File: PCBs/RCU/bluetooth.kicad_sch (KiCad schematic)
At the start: 14 parts

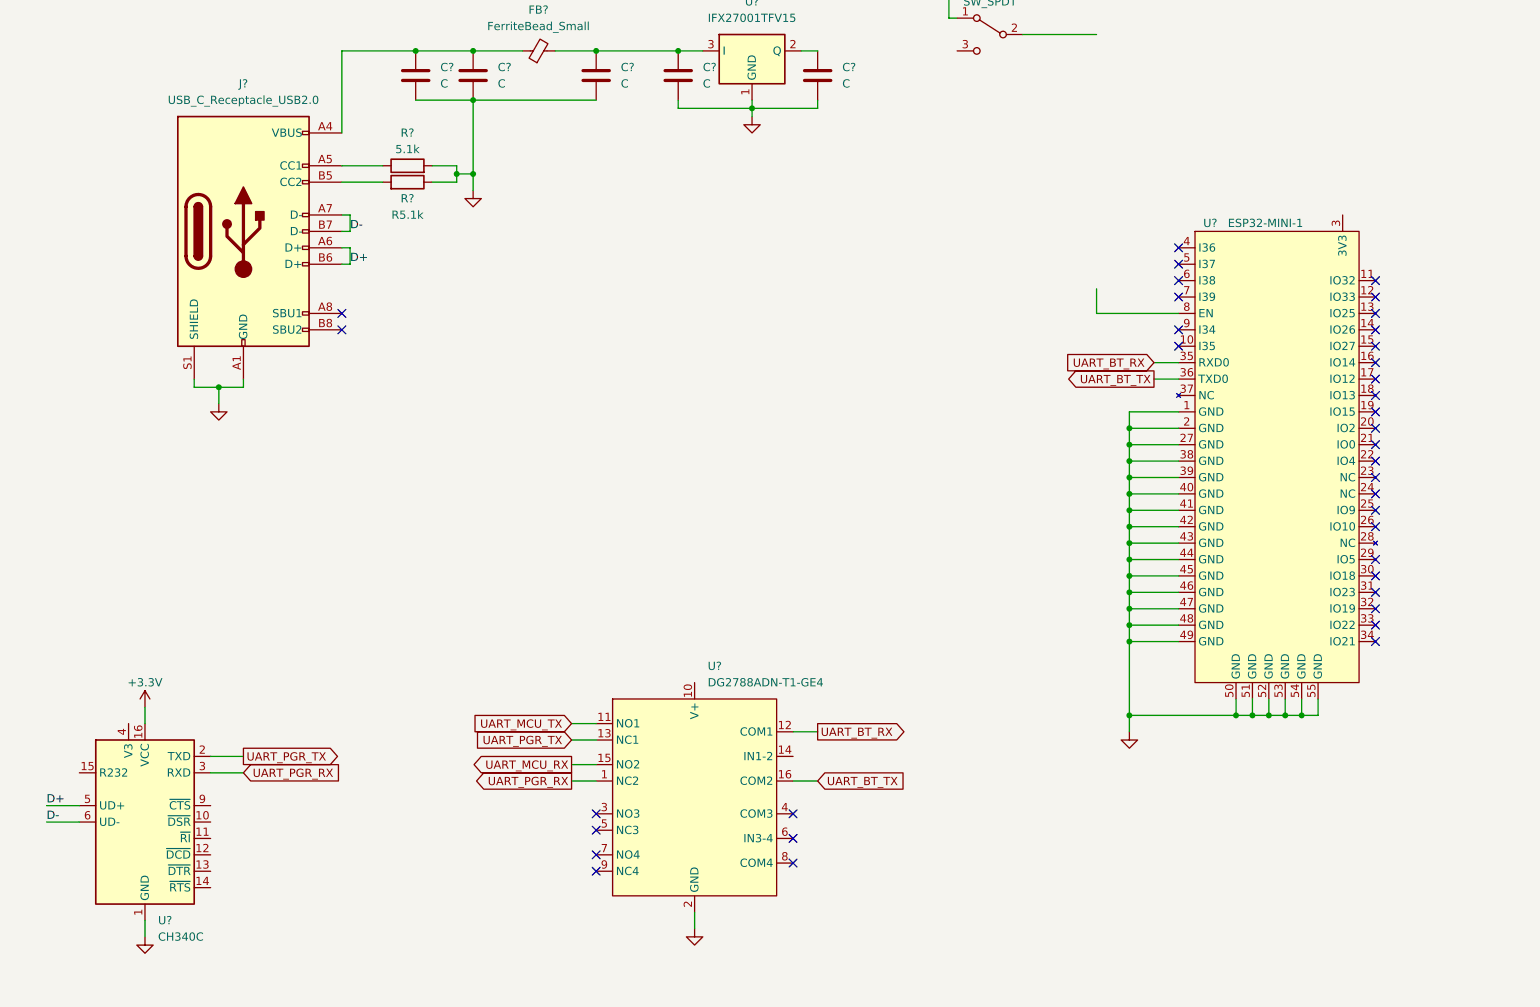
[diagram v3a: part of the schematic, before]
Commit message: Completed UART multiplexer circuit
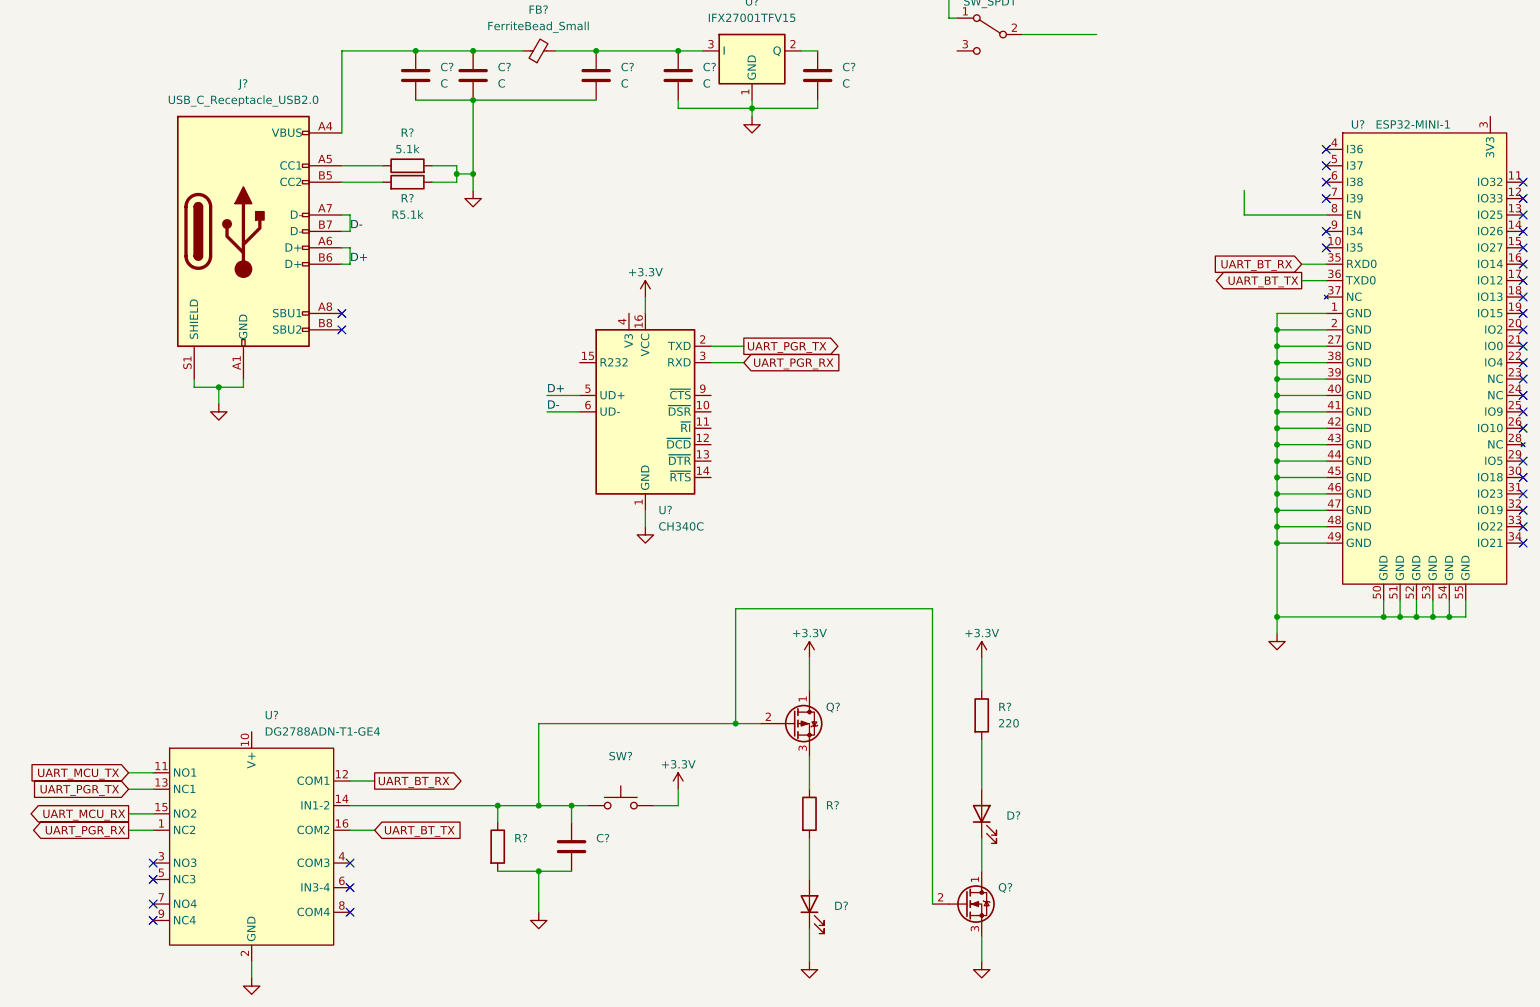
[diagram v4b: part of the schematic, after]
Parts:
- added C?: (no value), symbol Device:C
- added D? (x2): (no value), symbol Device:LED
- added Q?: (no value), symbol Device:Q_PMOS_DGS
- added Q?: (no value), symbol Device:Q_NMOS_DGS
- added R? (x2): (no value), symbol Device:R
- added R?: 220, symbol Device:R
- added SW?: (no value), symbol Switch:SW_Push
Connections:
- net +3V3: now also Q?.1 (D), R?.1, SW?.2
- net GND: now also C?.2, D?.1 (K), Q?.3 (S), R?.2
- net at U?.14 (IN1-2): now also C?.1, Q?.2 (G), Q?.2 (G), R?.1, SW?.1
- new net: Q?.3 (S), R?.1
- new net: D?.2 (A), R?.2 (x2)
- new net: D?.1 (K), Q?.1 (D)
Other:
- moved on the sheet: U?

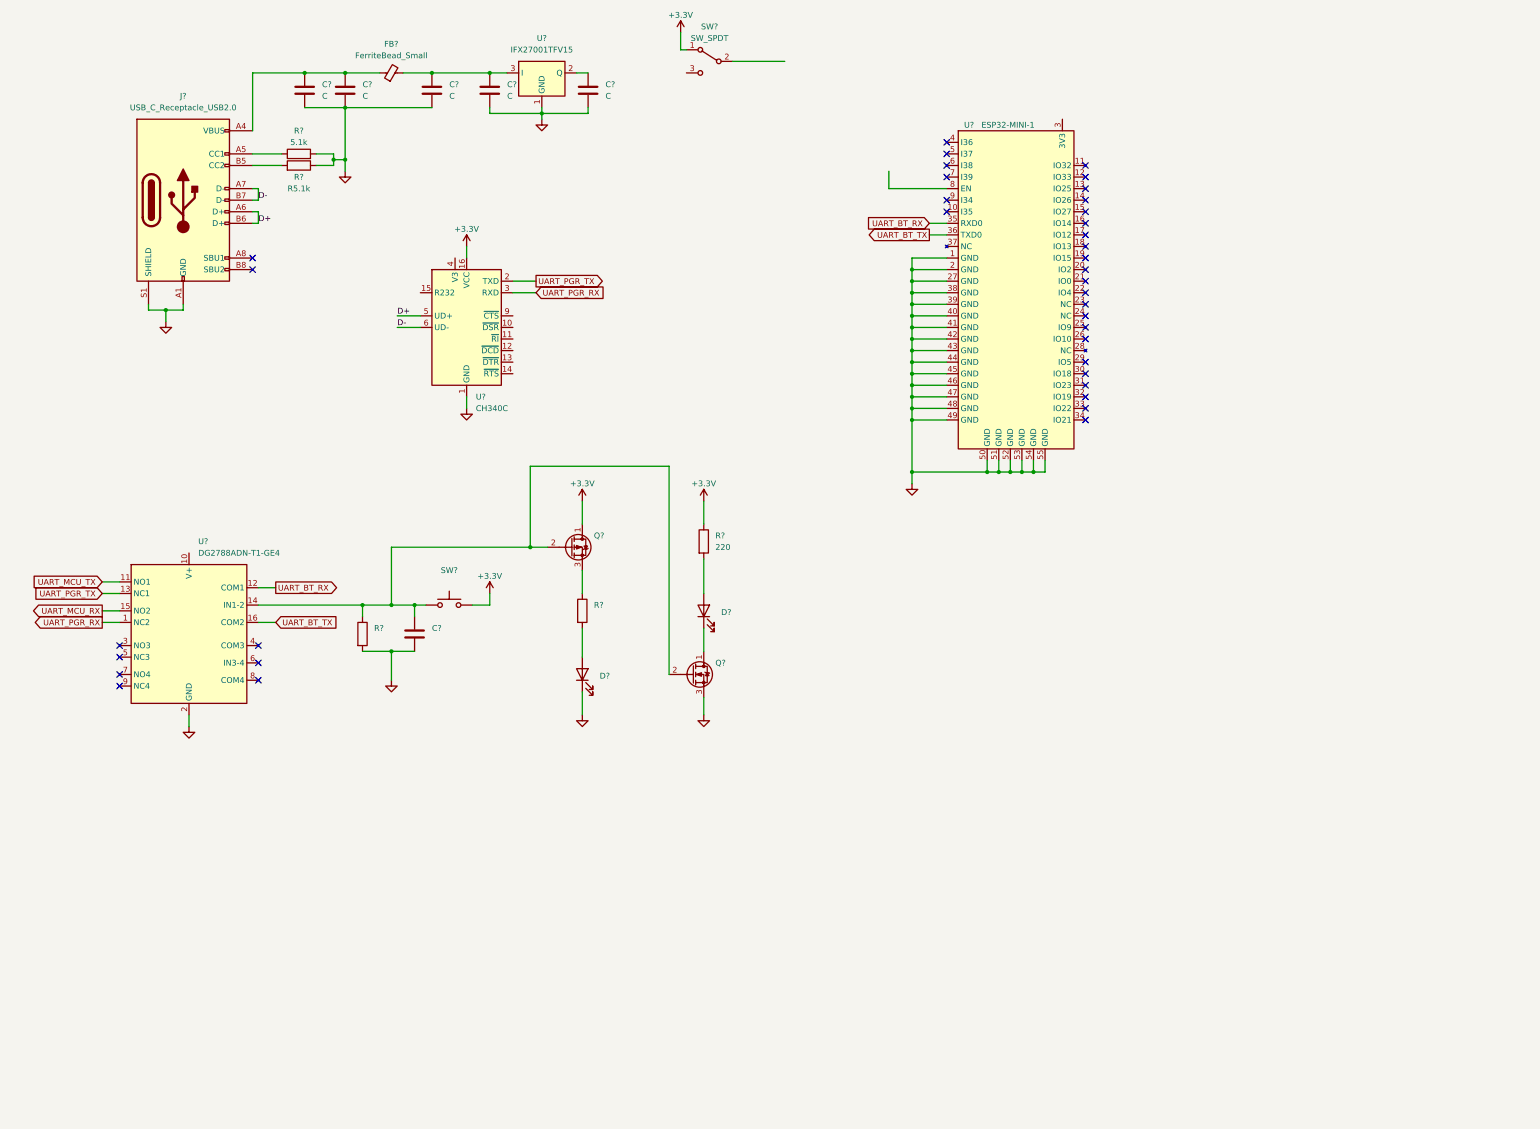
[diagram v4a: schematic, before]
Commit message: Complete ESP32 programming circuit
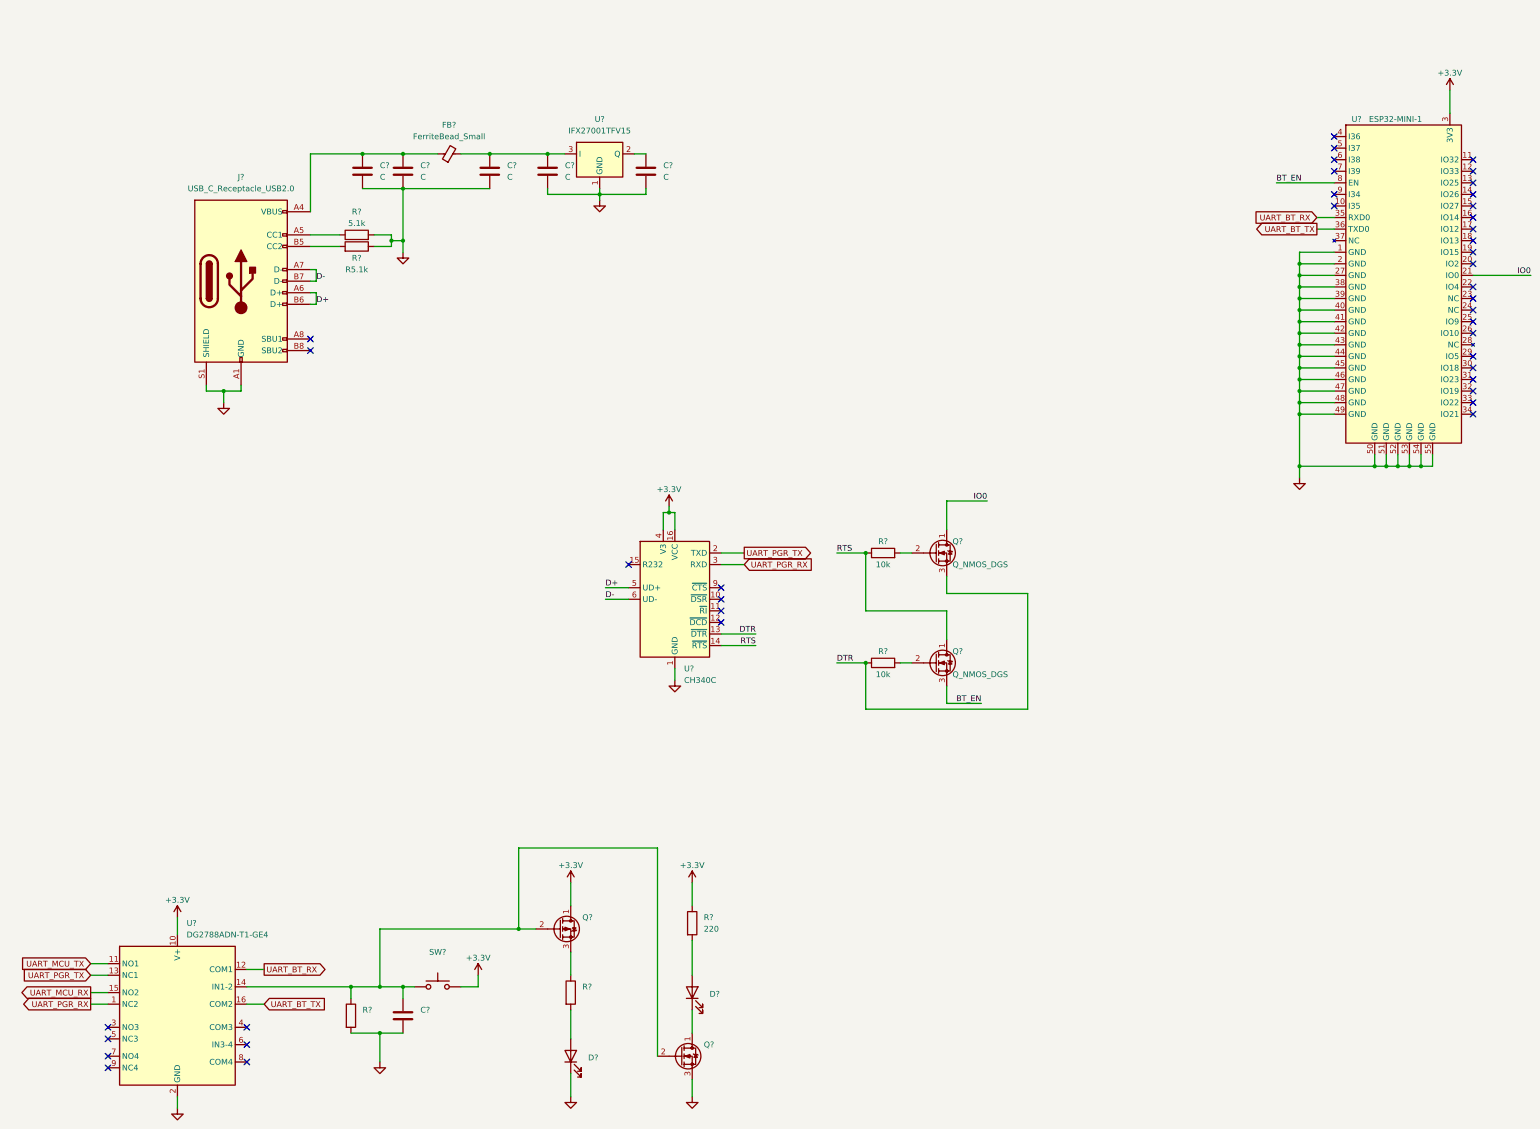
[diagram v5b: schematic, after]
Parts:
- removed SW?: SW_SPDT, symbol Switch:SW_SPDT
- added Q? (x2): Q_NMOS_DGS, symbol Device:Q_NMOS_DGS
- added R? (x2): 10k, symbol Device:R
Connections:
- net +3V3: now also U?.10 (V+), U?.3 (3V3), U?.4 (V3)
- net IO0: now reaches U?.21 (IO0)
- net IO0: now also Q?.1 (D)
- net BT_EN: now reaches U?.8 (EN)
- net BT_EN: now also Q?.3 (S)
- net DTR: now reaches U?.13 (~{DTR})
- net DTR: now also Q?.3 (S), R?.1
- net RTS: now reaches U?.14 (~{RTS})
- net RTS: now also Q?.1 (D), R?.1
- new net: Q?.2 (G), R?.2 (x2)
- no-connect marks 37 -> 41
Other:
- moved on the sheet: C?, D?, FB?, J?, Q?, R5.1k, R?, SW?, U?

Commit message: Finished Bluetooth schematic
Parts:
- removed C? (x5): C, symbol Device:C
- removed FB?: FerriteBead_Small, symbol Device:FerriteBead_Small
- removed U?: IFX27001TFV15, Package_TO_SOT_SMD:TO-252-3_TabPin2, symbol Regulator_Linear:IFX27001TFV15
- added C?: 0.1u, symbol Device:C
- added C? (x2): (no value), symbol Device:C
- added C?: 10u, symbol Device:C
- added D? (x2): LED, symbol Device:LED
- added D? (x4): D_TVS, symbol Device:D_TVS
- added D?: (no value), symbol Device:D_TVS
- added R? (x2): 220, symbol Device:R
- added R?: 10k, symbol Device:R
- C?: value (none) -> 0.1u
- D? (x2): value (none) -> LED
- Q?: value (none) -> Q_PMOS_DGS
- Q?: value (none) -> Q_NMOS_DGS
- R?: value (none) -> 10k
- R?: value (none) -> 220
- SW?: value (none) -> SW_Push
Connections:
- net +3V3: now also C?.1, C?.1, C?.1, R?.2
- net BT_EN: now also Q?.1 (D), C?.1, R?.1; no longer Q?.3 (S)
- net D+: now also D?.2 (A2)
- net D-: now also D?.2 (A2)
- net GND: now also C?.2, C?.2, C?.2, C?.2, D?.1 (A1), D?.1 (A1), D?.1 (A1), D?.1 (A1), D?.1 (A1), D?.1 (K), D?.1 (K)
- net RTS: now also Q?.3 (S); no longer Q?.1 (D)
- net VBUS2: now reaches J?.A4 (VBUS), J?.A9 (VBUS), J?.B4 (VBUS), J?.B9 (VBUS)
- net VBUS2: now also D?.2 (A2)
- net CC1: now reaches J?.A5 (CC1), R?.1
- net CC1: now also D?.2 (A2)
- net CC2: now reaches J?.B5 (CC2), R5.1k.2
- net CC2: now also D?.2 (A2)
- net at U?.11 (IO32): now also R?.1
- net at U?.12 (IO33): now also R?.1
- new net: D?.2 (A), R?.2 (x2)
- no-connect marks 41 -> 39
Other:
- note added: "Double Check Bypass values here!!"
- note added: "ESP32-Mini Bluetooth Module"
- note added: "Enabled"
- note added: "Powered On"
- note added: "Programming/Transcieving Selector"
- note added: "USB Type C Connector Schematic"
- note added: "USB to UART with CH340C"
- moved on the sheet: C?, D?, J?, Q?, R5.1k, R?, SW?, U?

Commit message: Finished Microcontroller schematic
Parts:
- C? (x2): value (none) -> 1u
- D?: value (none) -> D_TVS
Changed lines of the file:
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@@
       (effects (font (size 1.27 1.27)) (justify left))
     )
-    (property "Value" "" (id 1) (at 374.65 90.17 90)
+    (property "Value" "1u" (id 1) (at 374.65 90.17 90)
       (effects (font (size 1.27 1.27)) (justify left))
     )
@@
       (effects (font (size 1.27 1.27)) (justify left))
     )
-    (property "Value" "" (id 1) (at 285.75 129.54 0)
+    (property "Value" "1u" (id 1) (at 285.75 129.54 0)
       (effects (font (size 1.27 1.27)) (justify left))
     )
@@
       (effects (font (size 1.27 1.27)) (justify right))
     )
-    (property "Value" "" (id 1) (at 71.12 82.55 90)
-      (effects (font (size 1.27 1.27)) (justify right))
-    )
+    (property "Value" "D_TVS" (id 1) (at 71.12 82.55 90)
+      (effects (font (size 1.27 1.27)) (justify right))
+    )
